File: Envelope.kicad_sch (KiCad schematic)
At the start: 15 parts

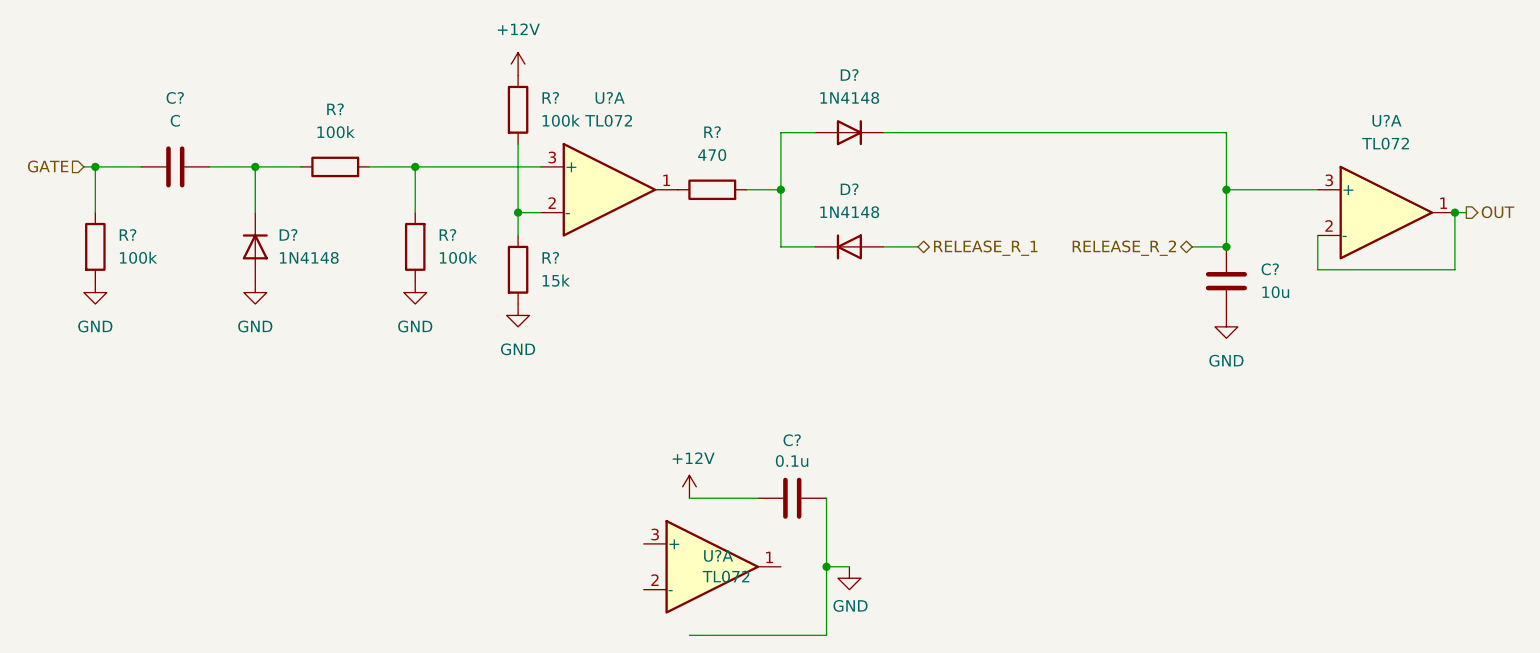
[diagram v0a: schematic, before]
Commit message: Finish schematic
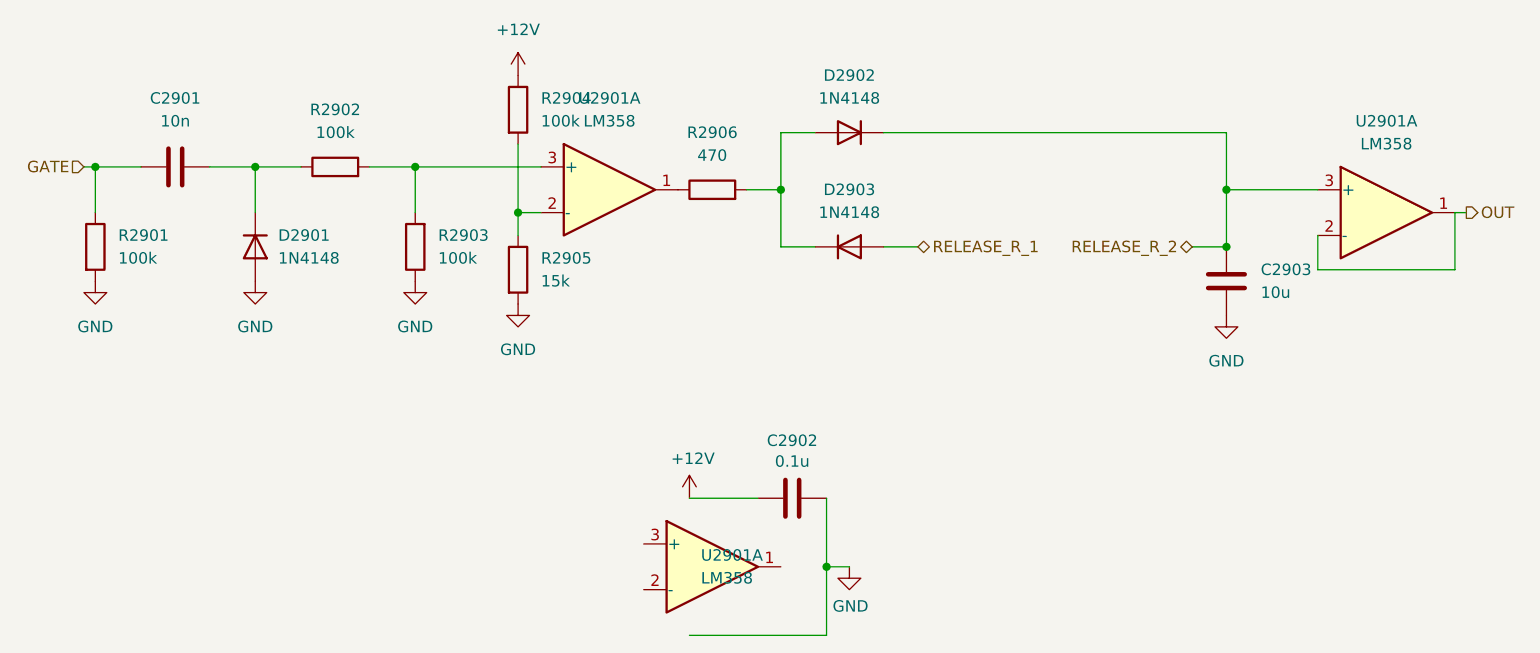
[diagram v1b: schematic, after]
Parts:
- removed U? (x2): TL072, symbol Amplifier_Operational:TL072
- removed U?: TL072, Package_DIP:DIP-8_W7.62mm_Socket, symbol Amplifier_Operational:TL072
- added U2901 (x3): LM358, Package_DIP:DIP-8_W7.62mm_Socket, symbol Amplifier_Operational:LM358
- C2901: renamed from C?; value C -> 10n; footprint (none) -> Capacitor_THT:C_Disc_D5.0mm_W2.5mm_P5.00mm
- C2903: renamed from C?; footprint (none) -> Capacitor_THT:C_Disc_D5.0mm_W2.5mm_P5.00mm
- R2901, R2902, R2903, R2904, R2905, R2906: renamed from R?; footprint (none) -> Resistor_THT:R_Axial_DIN0207_L6.3mm_D2.5mm_P7.62mm_Horizontal
- gave numbers to parts that had none: 4
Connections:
- net OUT: now also U2901.1, U2901.2 (-)
- net RELEASE_R_2: now also U2901.3 (+)
- net at R2902.2, R2903.2: now also U2901.3 (+)
- net at R2904.2, R2905.1: now also U2901.2 (-)
- net at R2906.1: now also U2901.1
